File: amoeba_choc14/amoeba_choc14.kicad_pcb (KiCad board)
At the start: 2 copper layers, 14 x 16 mm, 8 parts, among them J1 Conn_01x01_Pin, J2 Conn_01x01_Pin, J3 Conn_01x01_Pin, J4 Conn_01x01_Pin, SW1 SW_SPST

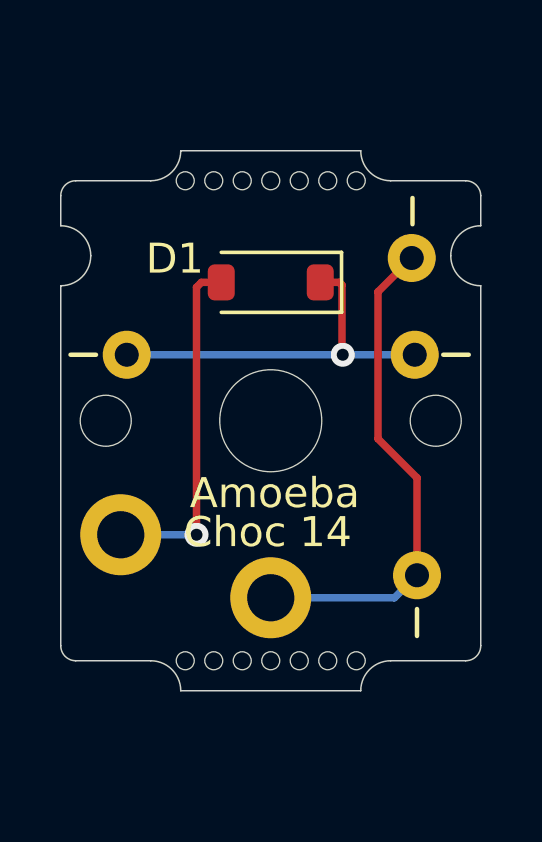
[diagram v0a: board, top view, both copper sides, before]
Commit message: feat(amoeba): extra column pad for MCU connection
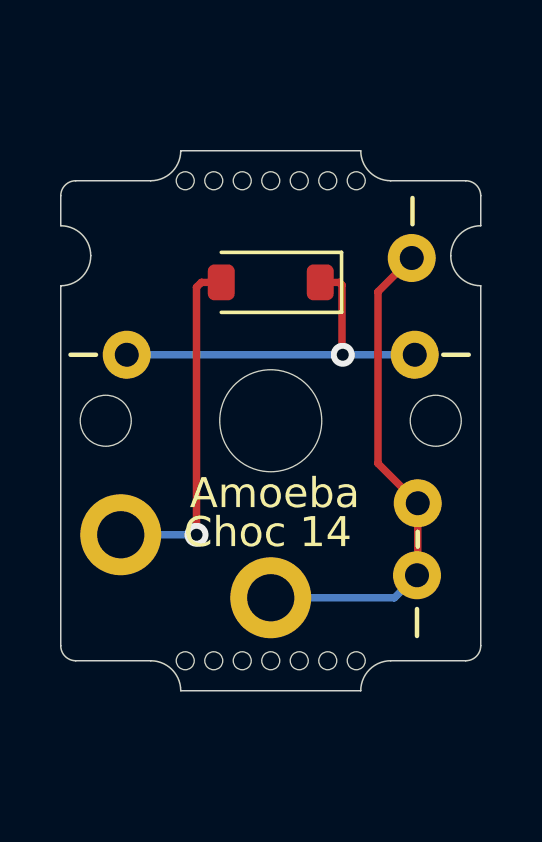
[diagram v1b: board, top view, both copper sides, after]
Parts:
- added J5: Conn_01x01_Pin, Amoeba_Choc_Nar:Pin_D0.8mm_L7.0mm, B.Cu at (134.9, 112.8)
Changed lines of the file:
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@@
 	(title_block
 		(title "Amoeba Choc 14")
-		(date "2024-02-22")
+		(date "2024-04-11")
 		(rev "0.1.0-alpha")
 		(comment 1 "and sturdier column walls; with socket STEP file. ")
@@
 			(at 3.2 0.7875 180)
 			(layer "F.SilkS")
+			(hide yes)
 			(effects
 				(font
@@
 	(footprint "Amoeba_Choc_Nar:Pin_D0.8mm_L7.0mm"
 		(layer "B.Cu")
+		(at 134.9 112.75 180)
+		(descr "solder Pin_ diameter 0.8mm, hole diameter 0.8mm (press fit), length 7.0mm")
+		(tags "solder Pin_ press fit")
+		(property "Reference" "J5"
+			(at -2.95 0.05 180)
+			(layer "B.Fab")
+			(effects
+				(font
+					(size 1 1)
+					(thickness 0.15)
+				)
+				(justify mirror)
+			)
+		)
+		(property "Value" "Conn_01x01_Pin"
+			(at 0 2.05 180)
+			(layer "B.Fab")
+			(hide yes)
+			(effects
+				(font
+					(size 1 1)
+					(thickness 0.15)
+				)
+				(justify mirror)
+			)
+		)
+		(property "Footprint" "Amoeba_Choc_Nar:Pin_D0.8mm_L7.0mm"
+			(at 0 0 0)
+			(unlocked yes)
+			(layer "B.Fab")
+			(hide yes)
+			(effects
+				(font
+					(size 1.27 1.27)
+				)
+				(justify mirror)
+			)
+		)
+		(property "Datasheet" ""
+			(at 0 0 0)
+			(unlocked yes)
+			(layer "B.Fab")
+			(hide yes)
+			(effects
+				(font
+					(size 1.27 1.27)
+				)
+				(justify mirror)
+			)
+		)
+		(property "Description" ""
+			(at 0 0 0)
+			(unlocked yes)
+			(layer "B.Fab")
+			(hide yes)
+			(effects
+				(font
+					(size 1.27 1.27)
+				)
+				(justify mirror)
+			)
+		)
+		(property "Config" "do not fit"
+			(at 0 0 0)
+			(unlocked yes)
+			(layer "B.Fab")
+			(hide yes)
+			(effects
+				(font
+					(size 1 1)
+					(thickness 0.15)
+				)
+				(justify mirror)
+			)
+		)
+		(property ki_fp_filters "Connector*:*_1x??_*")
+		(sheetname "Root")
+		(sheetfile "amoeba_choc14.kicad_sch")
+		(attr through_hole exclude_from_pos_files exclude_from_bom)
+		(fp_circle
+			(center 0 0)
+			(end 0.8 0)
+			(stroke
+				(width 0.12)
+				(type solid)
+			)
+			(fill none)
+			(layer "B.Fab")
+		)
+		(fp_circle
+			(center 0 0)
+			(end 0.5 0)
+			(stroke
+				(width 0.12)
+				(type solid)
+			)
+			(fill none)
+			(layer "B.Fab")
+		)
+		(fp_text user "${REFERENCE}"
+			(at 0 -0.3 180)
+			(layer "B.Fab")
+			(hide yes)
+			(effects
+				(font
+					(size 1 1)
+					(thickness 0.15)
+				)
+				(justify mirror)
+			)
+		)
+		(pad "1" thru_hole circle
+			(at 0 0 180)
+			(size 1.6 1.6)
+			(drill 0.8)
+			(layers "*.Cu" "*.Mask")
+			(remove_unused_layers no)
+			(net 3 "/col")
+			(pinfunction "Pin_1")
+			(pintype "passive")
+		)
+		(model "${KICAD6_3DMODEL_DIR}/Connector_Pin.3dshapes/Pin_D1.0mm_L10.0mm.wrl"
+			(offset
+				(xyz 0 0 0)
+			)
+			(scale
+				(xyz 0.8 0.8 0.7)
+			)
+			(rotate
+				(xyz 0 0 0)
+			)
+		)
+	)
+	(footprint "Amoeba_Choc_Nar:Pin_D0.8mm_L7.0mm"
+		(layer "B.Cu")
 		(at 134.7 104.575 180)
 		(descr "solder Pin_ diameter 0.8mm, hole diameter 0.8mm (press fit), length 7.0mm")
@@
 		)
 		(fp_text user "${REFERENCE}"
-			(at 1.8 -1 0)
+			(at -2.05 0.85 0)
 			(layer "B.Fab")
 			(effects
@@
 		)
 		(fp_text user "${REFERENCE}"
-			(at -1.4 -1 0)
+			(at 1.95 1.05 0)
 			(layer "B.Fab")
 			(effects
@@
 	)
 	(gr_line
+		(start 134.9 113.7)
+		(end 134.9 114.2)
+		(stroke
+			(width 0.15)
+			(type default)
+		)
+		(layer "B.SilkS")
+	)
+	(gr_line
 		(start 135.75 107.8)
 		(end 136.6 107.8)
@@
 			(type default)
 		)
+		(layer "B.SilkS")
+	)
+	(gr_rect
+		(start 124.3 102.4)
+		(end 130.8 106.2)
+		(stroke
+			(width 0.15)
+			(type solid)
+		)
+		(fill solid)
 		(layer "B.SilkS")
 	)
@@
 		(start 134.725 102.575)
 		(end 134.725 103.45)
+		(stroke
+			(width 0.15)
+			(type default)
+		)
+		(layer "F.SilkS")
+	)
+	(gr_line
+		(start 134.9 113.7)
+		(end 134.9 114.2)
 		(stroke
 			(width 0.15)
@@
 	)
 	(segment
+		(start 133.575 111.425)
+		(end 133.575 105.7)
+		(width 0.25)
+		(layer "F.Cu")
+		(net 3)
+	)
+	(segment
+		(start 134.9 112.75)
+		(end 134.9 115.125)
+		(width 0.25)
+		(layer "F.Cu")
+		(net 3)
+	)
+	(segment
+		(start 134.9 112.75)
+		(end 133.575 111.425)
+		(width 0.25)
+		(layer "F.Cu")
+		(net 3)
+	)
+	(segment
+		(start 134.9 115.125)
+		(end 134.875 115.15)
+		(width 0.25)
+		(layer "F.Cu")
+		(net 3)
+	)
+	(segment
 		(start 133.575 105.7)
 		(end 134.7 104.575)
 		(width 0.25)
 		(layer "F.Cu")
-		(net 3)
-	)
-	(segment
-		(start 134.875 115.15)
-		(end 134.875 111.9)
-		(width 0.25)
-		(layer "F.Cu")
-		(net 3)
-	)
-	(segment
-		(start 134.875 111.9)
-		(end 133.575 110.6)
-		(width 0.25)
-		(layer "F.Cu")
-		(net 3)
-	)
-	(segment
-		(start 133.575 110.6)
-		(end 133.575 105.7)
-		(width 0.25)
-		(layer "F.Cu")

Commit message: feat: width 13.7 mm, clearer row/col silk
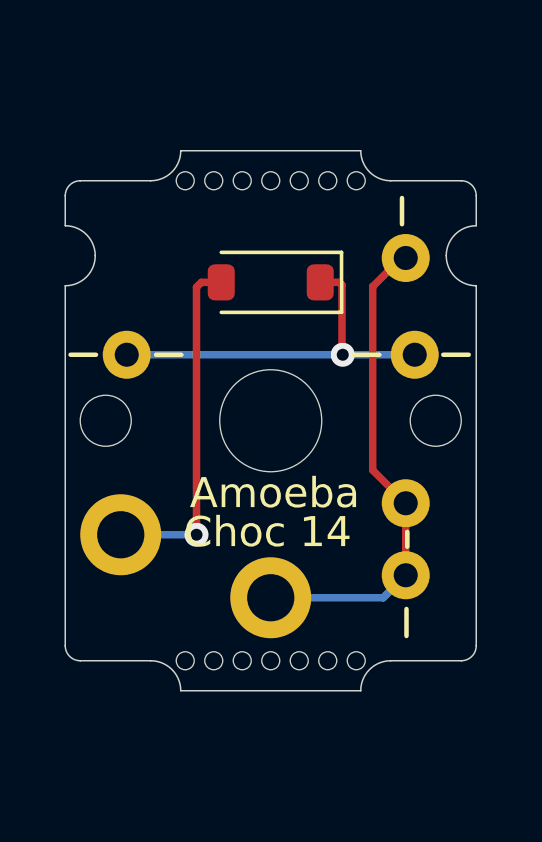
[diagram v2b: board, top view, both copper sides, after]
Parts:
- moved J5 0.40 mm to (134.5, 112.8)
- moved J2 0.38 mm to (134.5, 115.2)
- moved J1 0.20 mm to (134.5, 104.6)
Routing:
- net /col: track 16.8 -> 16.3 mm
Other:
- board size 14 x 16 mm -> 13.7 x 16 mm
- board text added: "choc spacing"
- board text added: "switch lower"

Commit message: feat: longer bite tabs for breakoff; mini ver num
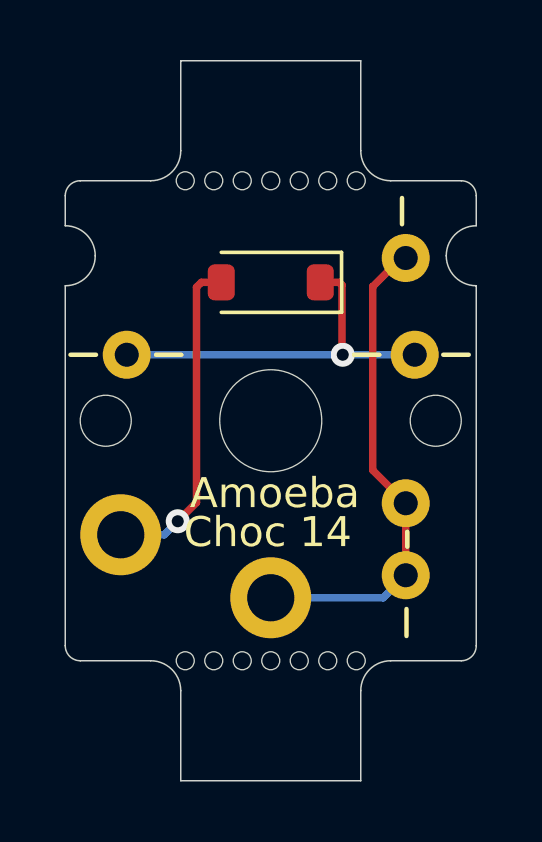
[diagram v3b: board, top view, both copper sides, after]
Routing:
- net Net-(D1-A): track 11.7 -> 11.0 mm
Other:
- board text added: "v010a1"
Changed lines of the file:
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@@
 	(title_block
 		(title "Amoeba Choc 14")
-		(date "2024-04-11")
-		(rev "0.1.0-alpha")
+		(date "2024-05-14")
+		(rev "0.1.0-alpha.1")
 		(comment 1 "and sturdier column walls; with socket STEP file. ")
 		(comment 2 "allows choc 18 mm or narrower Dactyl column spacing ")
@@
 		)
 		(property "Value" "1N4148"
-			(at 1.3 2.1875 180)
+			(at 0 4.7375 180)
 			(layer "F.Fab")
 			(effects
@@
 		)
 		(fp_text user "${REFERENCE}"
-			(at 0 -2 180)
+			(at -0.05 1.6875 180)
 			(layer "F.Fab")
 			(effects
@@
 			)
 		)
+		(sheetname "Root")
+		(sheetfile "amoeba_choc14.kicad_sch")
 		(attr through_hole exclude_from_pos_files exclude_from_bom)
 		(private_layers "Eco2.User" "User.9")
@@
 		(tags "solder Pin_ press fit")
 		(property "Reference" "J5"
-			(at -2.95 0.05 180)
+			(at -2.15 0 180)
 			(layer "B.Fab")
 			(effects
@@
 		)
 		(fp_text user "${REFERENCE}"
-			(at -1.7 0.05 0)
+			(at -2.25 0.025 0)
 			(layer "B.Fab")
 			(effects
@@
 		)
 		(fp_text user "${REFERENCE}"
-			(at -1.925 0.275 0)
+			(at -2.1 0 0)
 			(layer "B.Fab")
 			(effects
@@
 	)
 	(gr_line
-		(start 133 119)
+		(start 133 122)
+		(end 133 119)
+		(stroke
+			(width 0.05)
+			(type default)
+		)
+		(layer "Edge.Cuts")
+	)
+	(gr_line
+		(start 133 122)
+		(end 127 122)
+		(stroke
+			(width 0.05)
+			(type default)
+		)
+		(layer "Edge.Cuts")
+	)
+	(gr_line
+		(start 133 101)
+		(end 133 98)
+		(stroke
+			(width 0.05)
+			(type default)
+		)
+		(layer "Edge.Cuts")
+	)
+	(gr_line
+		(start 133 98)
+		(end 127 98)
+		(stroke
+			(width 0.05)
+			(type default)
+		)
+		(layer "Edge.Cuts")
+	)
+	(gr_line
+		(start 127 122)
 		(end 127 119)
 		(stroke
@@
 	)
 	(gr_line
-		(start 133 101)
-		(end 127 101)
+		(start 127 101)
+		(end 127 98)
 		(stroke
 			(width 0.05)
@@
 		)
 		(layer "User.9")
+	)
+	(gr_text "v010a1"
+		(at 132.8 113.45 0)
+		(layer "B.SilkS")
+		(effects
+			(font
+				(size 1 1)
+				(thickness 0.15)
+			)
+			(justify left bottom mirror)
+		)
 	)
 	(gr_text "Choc 14"
@@
 	)
 	(segment
-		(start 127.525 113.8)
-		(end 127.525 105.55)
-		(width 0.25)
-		(layer "F.Cu")
-		(net 2)
-	)
-	(segment
 		(start 127.6875 105.3875)
 		(end 128.35 105.3875)
@@
 		(net 2)
 	)
+	(segment
+		(start 126.9 113.35)
+		(end 127.525 112.725)
+		(width 0.25)
+		(layer "F.Cu")
+		(net 2)
+	)
+	(segment
+		(start 127.525 112.725)
+		(end 127.525 105.55)
+		(width 0.25)
+		(layer "F.Cu")
+		(net 2)
+	)
 	(via
-		(at 127.525 113.8)
+		(at 126.9 113.35)
 		(size 0.8)
 		(drill 0.4)
@@
 	)
 	(segment
-		(start 127.525 113.8)
+		(start 126.45 113.8)
 		(end 125 113.8)
 		(width 0.25)
 		(layer "B.Cu")
+		(net 2)
+	)
+	(segment
+		(start 126.9 113.35)
+		(end 126.45 113.8)
+		(width 0.25)
+		(layer "B.Cu")

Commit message: feat: use SOD-323 diode, as 123 out of stock
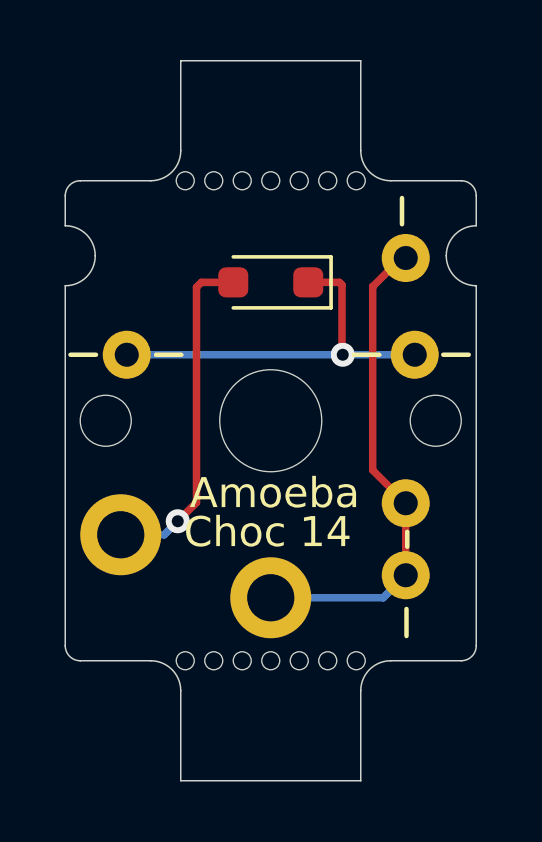
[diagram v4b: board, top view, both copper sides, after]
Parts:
- D1: footprint Diode_SMD:D_SOD-123 -> Diode_SMD:D_SOD-323_HandSoldering
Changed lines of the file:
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@@
 	(net 2 "Net-(D1-A)")
 	(net 3 "/col")
-	(footprint "Diode_SMD:D_SOD-123"
+	(footprint "Diode_SMD:D_SOD-323_HandSoldering"
 		(layer "F.Cu")
 		(at 130 105.3875 180)
-		(descr "SOD-123")
-		(tags "SOD-123")
+		(descr "SOD-323")
+		(tags "SOD-323")
 		(property "Reference" "D1"
-			(at 3.2 0.7875 180)
-			(layer "F.SilkS")
-			(hide yes)
+			(at 0 1.7875 180)
+			(layer "F.Fab")
 			(effects
 				(font
@@
 		)
 		(property "Value" "1N4148"
-			(at 0 4.7375 180)
-			(layer "F.Fab")
-			(effects
-				(font
-					(size 1 1)
-					(thickness 0.15)
-				)
-			)
-		)
-		(property "Footprint" "Diode_SMD:D_SOD-123"
+			(at 0 4.5875 180)
+			(layer "F.Fab")
+			(effects
+				(font
+					(size 1 1)
+					(thickness 0.15)
+				)
+			)
+		)
+		(property "Footprint" "Diode_SMD:D_SOD-323_HandSoldering"
 			(at 0 0 180)
 			(unlocked yes)
@@
 		(attr smd)
 		(fp_line
-			(start -2.36 1)
-			(end 1.65 1)
+			(start -2.01 0.85)
+			(end 1.25 0.85)
 			(stroke
 				(width 0.12)
@@
 		)
 		(fp_line
-			(start -2.36 -1)
-			(end 1.65 -1)
+			(start -2.01 -0.85)
+			(end 1.25 -0.85)
 			(stroke
 				(width 0.12)
@@
 		)
 		(fp_line
-			(start -2.36 -1)
-			(end -2.36 1)
+			(start -2.01 -0.85)
+			(end -2.01 0.85)
 			(stroke
 				(width 0.12)
@@
 		)
 		(fp_line
-			(start 2.35 1.15)
-			(end -2.35 1.15)
+			(start 2 -0.95)
+			(end 2 0.95)
 			(stroke
 				(width 0.05)
@@
 		)
 		(fp_line
-			(start 2.35 -1.15)
-			(end 2.35 1.15)
+			(start -2 0.95)
+			(end 2 0.95)
 			(stroke
 				(width 0.05)
@@
 		)
 		(fp_line
-			(start -2.35 -1.15)
-			(end 2.35 -1.15)
+			(start -2 -0.95)
+			(end 2 -0.95)
 			(stroke
 				(width 0.05)
@@
 		)
 		(fp_line
-			(start -2.35 -1.15)
-			(end -2.35 1.15)
+			(start -2 -0.95)
+			(end -2 0.95)
 			(stroke
 				(width 0.05)
@@
 		)
 		(fp_line
-			(start 1.4 0.9)
-			(end -1.4 0.9)
-			(stroke
-				(width 0.1)
-				(type solid)
-			)
-			(layer "F.Fab")
-		)
-		(fp_line
-			(start 1.4 -0.9)
-			(end 1.4 0.9)
-			(stroke
-				(width 0.1)
-				(type solid)
-			)
-			(layer "F.Fab")
-		)
-		(fp_line
-			(start 0.25 0.4)
-			(end -0.35 0)
-			(stroke
-				(width 0.1)
-				(type solid)
-			)
-			(layer "F.Fab")
-		)
-		(fp_line
-			(start 0.25 0)
-			(end 0.75 0)
-			(stroke
-				(width 0.1)
-				(type solid)
-			)
-			(layer "F.Fab")
-		)
-		(fp_line
-			(start 0.25 -0.4)
-			(end 0.25 0.4)
-			(stroke
-				(width 0.1)
-				(type solid)
-			)
-			(layer "F.Fab")
-		)
-		(fp_line
-			(start -0.35 0)
-			(end 0.25 -0.4)
-			(stroke
-				(width 0.1)
-				(type solid)
-			)
-			(layer "F.Fab")
-		)
-		(fp_line
-			(start -0.35 0)
-			(end -0.35 0.55)
-			(stroke
-				(width 0.1)
-				(type solid)
-			)
-			(layer "F.Fab")
-		)
-		(fp_line
-			(start -0.35 0)
-			(end -0.35 -0.55)
-			(stroke
-				(width 0.1)
-				(type solid)
-			)
-			(layer "F.Fab")
-		)
-		(fp_line
-			(start -0.75 0)
-			(end -0.35 0)
-			(stroke
-				(width 0.1)
-				(type solid)
-			)
-			(layer "F.Fab")
-		)
-		(fp_line
-			(start -1.4 0.9)
-			(end -1.4 -0.9)
-			(stroke
-				(width 0.1)
-				(type solid)
-			)
-			(layer "F.Fab")
-		)
-		(fp_line
-			(start -1.4 -0.9)
-			(end 1.4 -0.9)
-			(stroke
-				(width 0.1)
-				(type solid)
-			)
-			(layer "F.Fab")
-		)
-		(fp_text user "${REFERENCE}"
-			(at -0.05 1.6875 180)
-			(layer "F.Fab")
-			(effects
-				(font
-					(size 1 1)
-					(thickness 0.15)
-				)
-			)
+			(start 0.9 0.7)
+			(end -0.9 0.7)
+			(stroke
+				(width 0.1)
+				(type solid)
+			)
+			(layer "F.Fab")
+		)
+		(fp_line
+			(start 0.9 -0.7)
+			(end 0.9 0.7)
+			(stroke
+				(width 0.1)
+				(type solid)
+			)
+			(layer "F.Fab")
+		)
+		(fp_line
+			(start 0.2 0.35)
+			(end -0.3 0)
+			(stroke
+				(width 0.1)
+				(type solid)
+			)
+			(layer "F.Fab")
+		)
+		(fp_line
+			(start 0.2 0)
+			(end 0.45 0)
+			(stroke
+				(width 0.1)
+				(type solid)
+			)
+			(layer "F.Fab")
+		)
+		(fp_line
+			(start 0.2 -0.35)
+			(end 0.2 0.35)
+			(stroke
+				(width 0.1)
+				(type solid)
+			)
+			(layer "F.Fab")
+		)
+		(fp_line
+			(start -0.3 0)
+			(end 0.2 -0.35)
+			(stroke
+				(width 0.1)
+				(type solid)
+			)
+			(layer "F.Fab")
+		)
+		(fp_line
+			(start -0.3 0)
+			(end -0.5 0)
+			(stroke
+				(width 0.1)
+				(type solid)
+			)
+			(layer "F.Fab")
+		)
+		(fp_line
+			(start -0.3 -0.35)
+			(end -0.3 0.35)
+			(stroke
+				(width 0.1)
+				(type solid)
+			)
+			(layer "F.Fab")
+		)
+		(fp_line
+			(start -0.9 0.7)
+			(end -0.9 -0.7)
+			(stroke
+				(width 0.1)
+				(type solid)
+			)
+			(layer "F.Fab")
+		)
+		(fp_line
+			(start -0.9 -0.7)
+			(end 0.9 -0.7)
+			(stroke
+				(width 0.1)
+				(type solid)
+			)
+			(layer "F.Fab")
 		)
 		(pad "1" smd roundrect
-			(at -1.65 0 180)
-			(size 0.9 1.2)
+			(at -1.25 0 180)
+			(size 1 1)
 			(layers "F.Cu" "F.Paste" "F.Mask")
 			(roundrect_rratio 0.25)
@@
 		)
 		(pad "2" smd roundrect
-			(at 1.65 0 180)
-			(size 0.9 1.2)
+			(at 1.25 0 180)
+			(size 1 1)
 			(layers "F.Cu" "F.Paste" "F.Mask")
 			(roundrect_rratio 0.25)
@@
 			(pintype "passive")
 		)
-		(model "${KICAD8_3DMODEL_DIR}/Diode_SMD.3dshapes/D_SOD-123.wrl"
+		(model "${KICAD8_3DMODEL_DIR}/Diode_SMD.3dshapes/D_SOD-323.wrl"
 			(offset
 				(xyz 0 0 0)
@@
 	)
 	(segment
-		(start 132.2875 105.3875)
-		(end 131.65 105.3875)
+		(start 132.375 107.775)
+		(end 132.375 105.475)
 		(width 0.25)
 		(layer "F.Cu")
@@
 	)
 	(segment
-		(start 132.375 107.775)
-		(end 132.375 105.475)
+		(start 132.2875 105.3875)
+		(end 131.25 105.3875)
 		(width 0.25)
 		(layer "F.Cu")
@@
 	)
 	(segment
-		(start 127.6875 105.3875)
-		(end 128.35 105.3875)
+		(start 127.525 112.725)
+		(end 127.525 105.55)
 		(width 0.25)
 		(layer "F.Cu")
@@
 	)
 	(segment
-		(start 127.525 105.55)
-		(end 127.6875 105.3875)
+		(start 127.6875 105.3875)
+		(end 128.75 105.3875)
 		(width 0.25)
 		(layer "F.Cu")
@@
 	)
 	(segment
-		(start 127.525 112.725)
-		(end 127.525 105.55)
+		(start 127.525 105.55)
+		(end 127.6875 105.3875)
 		(width 0.25)
 		(layer "F.Cu")
